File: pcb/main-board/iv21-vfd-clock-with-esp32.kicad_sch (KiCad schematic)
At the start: 24 parts, among them J1 Conn_02x10_Odd_Even, J2 4328, P1 USB_C_Plug_USB2.0, SW1 SW_SPST, SW2 SW_SPST, U1 MAX6921AQI_, U2 MOUDLE-SEEEDUINO-XIAO-ESP32C3, U3 AP3012, U4 S-1167B24

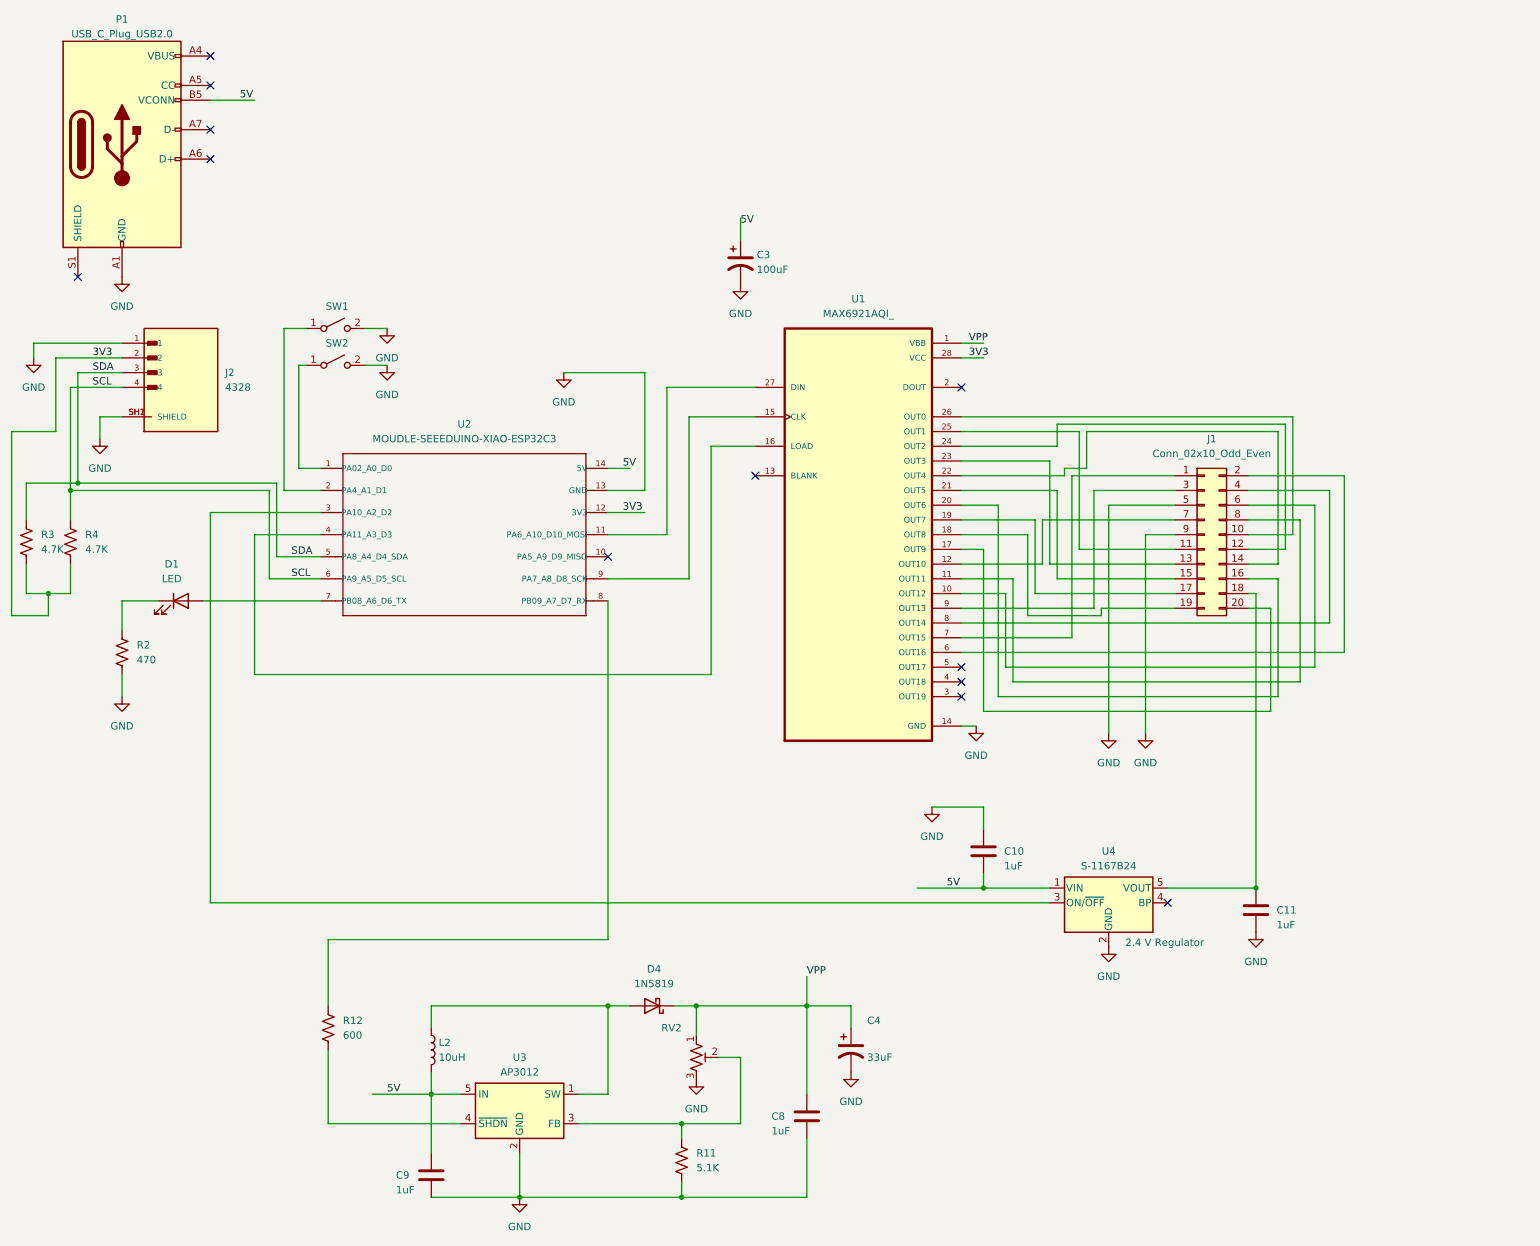
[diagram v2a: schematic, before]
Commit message: Move USB-C port closer to edge of board. Move USB-C port schematic symbol to inside of drawing border.
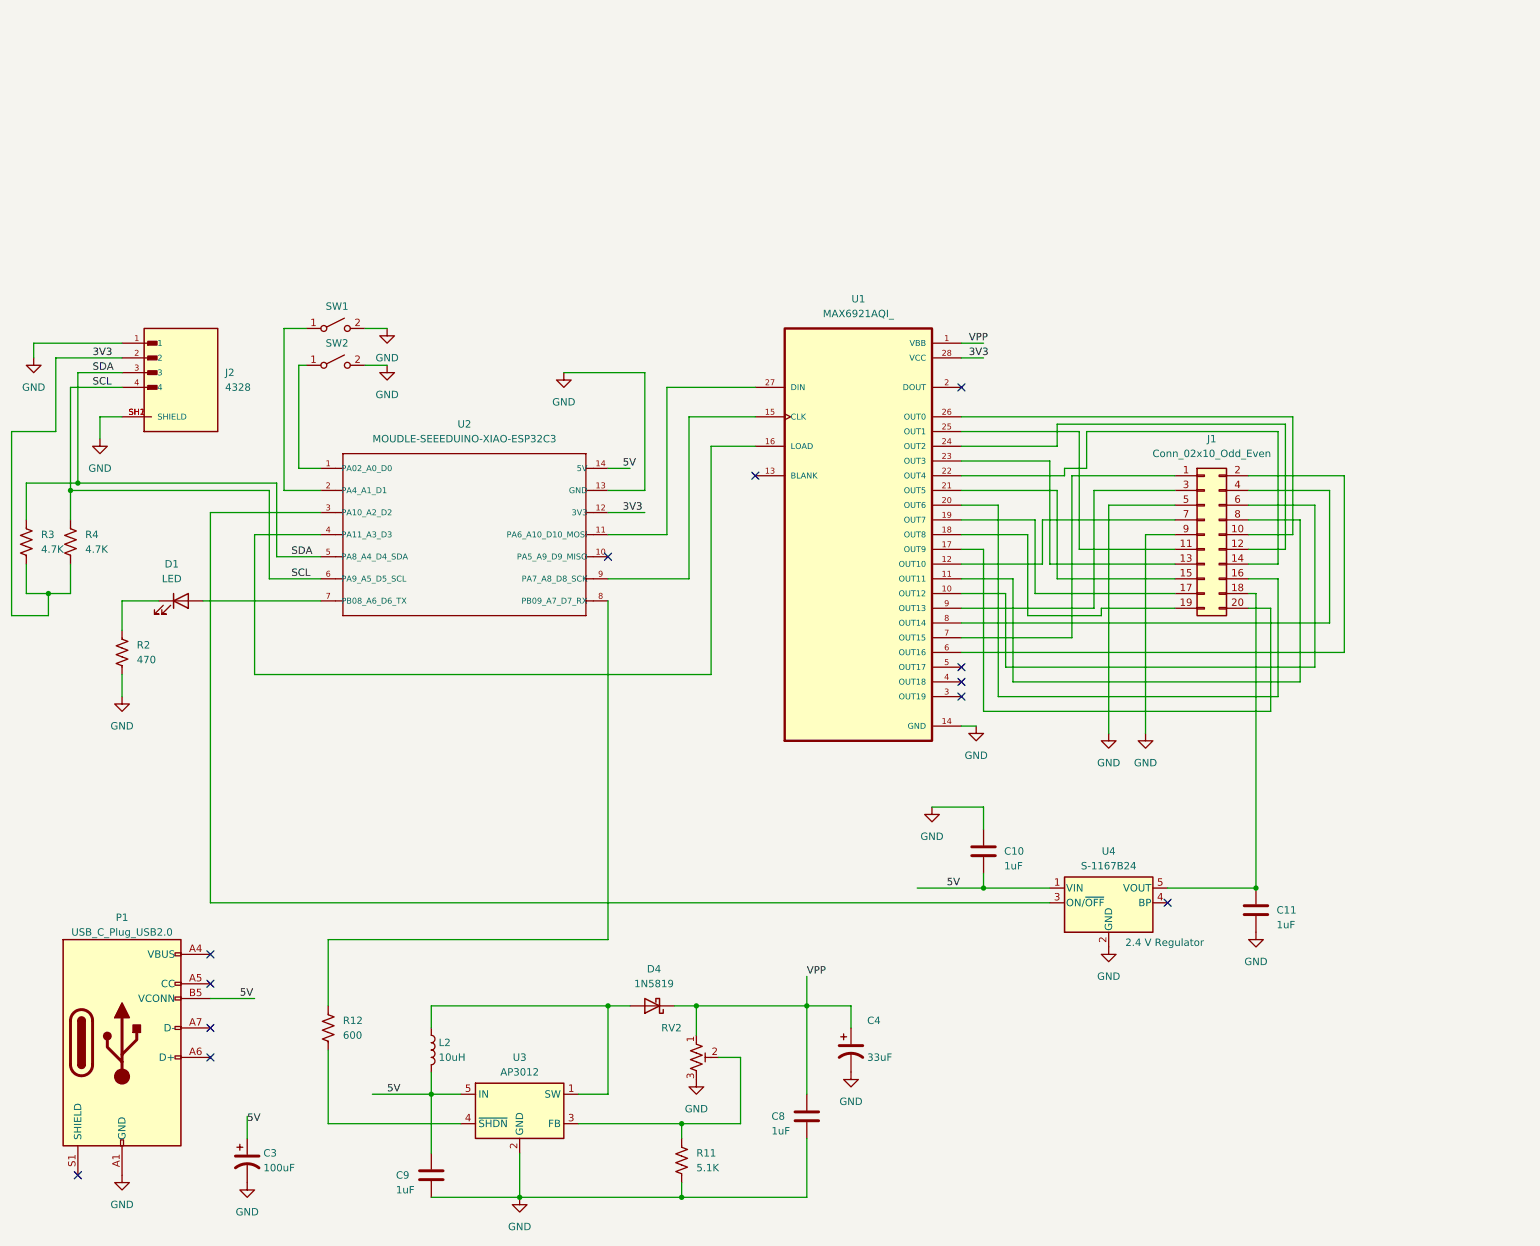
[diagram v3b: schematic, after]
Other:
- moved on the sheet: C3, P1
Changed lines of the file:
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@@
 	)
 	(no_connect
-		(at 48.26 7.62)
+		(at 48.26 162.56)
 	)
 	(no_connect
-		(at 25.4 27.94)
+		(at 25.4 182.88)
 	)
 	(no_connect
@@
 	)
 	(no_connect
-		(at 48.26 2.54)
+		(at 48.26 157.48)
 	)
 	(no_connect
@@
 	)
 	(no_connect
-		(at 48.26 -5.08)
+		(at 48.26 149.86)
 	)
 	(no_connect
-		(at 48.26 -10.16)
+		(at 48.26 144.78)
 	)
 	(no_connect
@@
 	(wire
 		(pts
-			(xy 139.7 17.78) (xy 139.7 21.59)
+			(xy 54.61 172.72) (xy 54.61 176.53)
 		)
 		(stroke
@@
 	(wire
 		(pts
-			(xy 48.26 -2.54) (xy 55.88 -2.54)
+			(xy 48.26 152.4) (xy 55.88 152.4)
 		)
 		(stroke
@@
 	)
 	(label "5V"
-		(at 53.34 -2.54 0)
+		(at 53.34 152.4 0)
 		(effects
 			(font
@@
 	)
 	(label "5V"
-		(at 139.7 19.05 0)
+		(at 54.61 173.99 0)
 		(effects
 			(font
@@
 	(symbol
 		(lib_id "power:GND")
-		(at 33.02 27.94 0)
+		(at 33.02 182.88 0)
 		(unit 1)
 		(exclude_from_sim no)
@@
 		(fields_autoplaced yes)
 		(property "Reference" "#PWR020"
-			(at 33.02 34.29 0)
+			(at 33.02 189.23 0)
 			(effects
 				(font
@@
 		)
 		(property "Value" "GND"
-			(at 33.02 33.02 0)
+			(at 33.02 187.96 0)
 			(effects
 				(font
@@
 		)
 		(property "Footprint" ""
-			(at 33.02 27.94 0)
+			(at 33.02 182.88 0)
 			(effects
 				(font
@@
 		)
 		(property "Datasheet" ""
-			(at 33.02 27.94 0)
+			(at 33.02 182.88 0)
 			(effects
 				(font
@@
 		)
 		(property "Description" "Power symbol creates a global label with name \"GND\" , ground"
-			(at 33.02 27.94 0)
+			(at 33.02 182.88 0)
 			(effects
 				(font
@@
 	(symbol
 		(lib_id "Connector:USB_C_Plug_USB2.0")
-		(at 33.02 5.08 0)
+		(at 33.02 160.02 0)
 		(unit 1)
 		(exclude_from_sim no)
@@
 		(fields_autoplaced yes)
 		(property "Reference" "P1"
-			(at 33.02 -16.51 0)
+			(at 33.02 138.43 0)
 			(effects
 				(font
@@
 		)
 		(property "Value" "USB_C_Plug_USB2.0"
-			(at 33.02 -13.97 0)
+			(at 33.02 140.97 0)
 			(effects
 				(font
@@
 		)
 		(property "Footprint" "Connector_USB:USB_C_Receptacle_GCT_USB4105-xx-A_16P_TopMnt_Horizontal"
-			(at 36.83 5.08 0)
+			(at 36.83 160.02 0)
 			(effects
 				(font
@@
 		)
 		(property "Datasheet" "https://www.usb.org/sites/default/files/documents/usb_type-c.zip"
-			(at 36.83 5.08 0)
+			(at 36.83 160.02 0)
 			(effects
 				(font
@@
 		)
 		(property "Description" "USB 2.0-only Type-C Plug connector"
-			(at 33.02 5.08 0)
+			(at 33.02 160.02 0)
 			(effects
 				(font
@@
 	(symbol
 		(lib_id "Device:C_Polarized_US")
-		(at 139.7 25.4 0)
+		(at 54.61 180.34 0)
 		(unit 1)
 		(exclude_from_sim no)
@@
 		(dnp no)
 		(property "Reference" "C3"
-			(at 142.494 24.13 0)
+			(at 57.404 179.07 0)
 			(effects
 				(font
@@
 		)
 		(property "Value" "100uF"
-			(at 142.494 26.67 0)
+			(at 57.404 181.61 0)
 			(effects
 				(font
@@
 		)
 		(property "Footprint" "Capacitor_SMD:CP_Elec_8x10.5"
-			(at 139.7 25.4 0)
+			(at 54.61 180.34 0)
 			(effects
 				(font
@@
 		)
 		(property "Datasheet" "~"
-			(at 139.7 25.4 0)
+			(at 54.61 180.34 0)
 			(effects
 				(font
@@
 		)
 		(property "Description" "Polarized capacitor, US symbol"
-			(at 139.7 25.4 0)
+			(at 54.61 180.34 0)
 			(effects
 				(font
@@
 	(symbol
 		(lib_id "power:GND")
-		(at 139.7 29.21 0)
+		(at 54.61 184.15 0)
 		(unit 1)
 		(exclude_from_sim no)
@@
 		(fields_autoplaced yes)
 		(property "Reference" "#PWR016"
-			(at 139.7 35.56 0)
+			(at 54.61 190.5 0)
 			(effects
 				(font
@@
 		)
 		(property "Value" "GND"
-			(at 139.7 34.29 0)
+			(at 54.61 189.23 0)
 			(effects
 				(font
@@
 		)
 		(property "Footprint" ""
-			(at 139.7 29.21 0)
+			(at 54.61 184.15 0)
 			(effects
 				(font
@@
 		)
 		(property "Datasheet" ""
-			(at 139.7 29.21 0)
+			(at 54.61 184.15 0)
 			(effects
 				(font
@@
 		)
 		(property "Description" "Power symbol creates a global label with name \"GND\" , ground"
-			(at 139.7 29.21 0)
+			(at 54.61 184.15 0)
 			(effects
 				(font

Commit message: - Add details to electrolytic capacitor components. - No-fill zone for inductor footprint
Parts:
- C3: Product URL (none) -> https://www.mouser.com/ProductDetail/581-AHA0810101M035R; Voltage Rating (none) -> 35V DC
- C4: Product URL (none) -> https://www.mouser.com/ProductDetail/581-AHA0810330M063R; Voltage Rating (none) -> 63V DC
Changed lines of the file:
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@@
 			)
 		)
-		(property "Datasheet" "~"
+		(property "Datasheet" "https://www.mouser.com/datasheet/2/40/kyocera_avx_aha_series-2887216.pdf"
 			(at 54.61 180.34 0)
 			(effects
@@
 		)
 		(property "Description" "Polarized capacitor, US symbol"
+			(at 54.61 180.34 0)
+			(effects
+				(font
+					(size 1.27 1.27)
+				)
+				(hide yes)
+			)
+		)
+		(property "Voltage Rating" "35V DC"
+			(at 54.61 180.34 0)
+			(effects
+				(font
+					(size 1.27 1.27)
+				)
+				(hide yes)
+			)
+		)
+		(property "Product URL" "https://www.mouser.com/ProductDetail/581-AHA0810101M035R"
 			(at 54.61 180.34 0)
 			(effects
@@
 			)
 		)
-		(property "Datasheet" "~"
+		(property "Datasheet" "https://www.mouser.com/datasheet/2/40/kyocera_avx_aha_series-2887216.pdf"
 			(at 158.75 161.29 0)
 			(effects
@@
 			(at 158.75 161.29 0)
 			(effects
+				(font
+					(size 1.27 1.27)
+				)
+				(hide yes)
+			)
+		)
+		(property "Voltage Rating" "63V DC"
+			(at 158.75 161.29 0)
+			(effects
+				(font
+					(size 1.27 1.27)
+				)
+				(hide yes)
+			)
+		)
+		(property "Product URL" "https://www.mouser.com/ProductDetail/581-AHA0810330M063R"
+			(at 158.75 161.29 0)
+			(effects

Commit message: Update some footprints and symbols in schematic.
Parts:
- P1: Product URL (none) -> https://www.mouser.com/ProductDetail/179-UJ20CHGSMT1P16TR
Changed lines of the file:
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@@
 			)
 		)
-		(property "Datasheet" "https://www.usb.org/sites/default/files/documents/usb_type-c.zip"
+		(property "Datasheet" "https://www.mouser.com/datasheet/2/1628/uj20_c_h_g_smt_1_p16_tr-3511223.pdf"
 			(at 36.83 160.02 0)
 			(effects
@@
 		)
 		(property "Description" "USB 2.0-only Type-C Plug connector"
+			(at 33.02 160.02 0)
+			(effects
+				(font
+					(size 1.27 1.27)
+				)
+				(hide yes)
+			)
+		)
+		(property "Product URL" "https://www.mouser.com/ProductDetail/179-UJ20CHGSMT1P16TR"
 			(at 33.02 160.02 0)
 			(effects
@@
 		(dnp no)
 		(property "Reference" "RV2"
-			(at 129.54 157.4799 0)
+			(at 129.032 161.29 0)
 			(effects
 				(font
@@
 		)
 		(property "Value" "100K"
-			(at 149.606 170.18 0)
+			(at 129.54 163.5761 0)
 			(effects
 				(font
@@
 				)
 				(justify right)
-				(hide yes)
-			)
-		)
+			)
+		)

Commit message: ...
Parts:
- L2: footprint Inductor_THT:L_Radial_D12.0mm_P5.00mm_Fastron_11P -> Inductor_THT:L_Radial_D7.5mm_P3.50mm_Fastron_07P
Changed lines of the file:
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@@
 			)
 		)
-		(property "Footprint" "Inductor_THT:L_Radial_D12.0mm_P5.00mm_Fastron_11P"
+		(property "Footprint" "Inductor_THT:L_Radial_D7.5mm_P3.50mm_Fastron_07P"
 			(at 86.36 161.29 0)
 			(effects

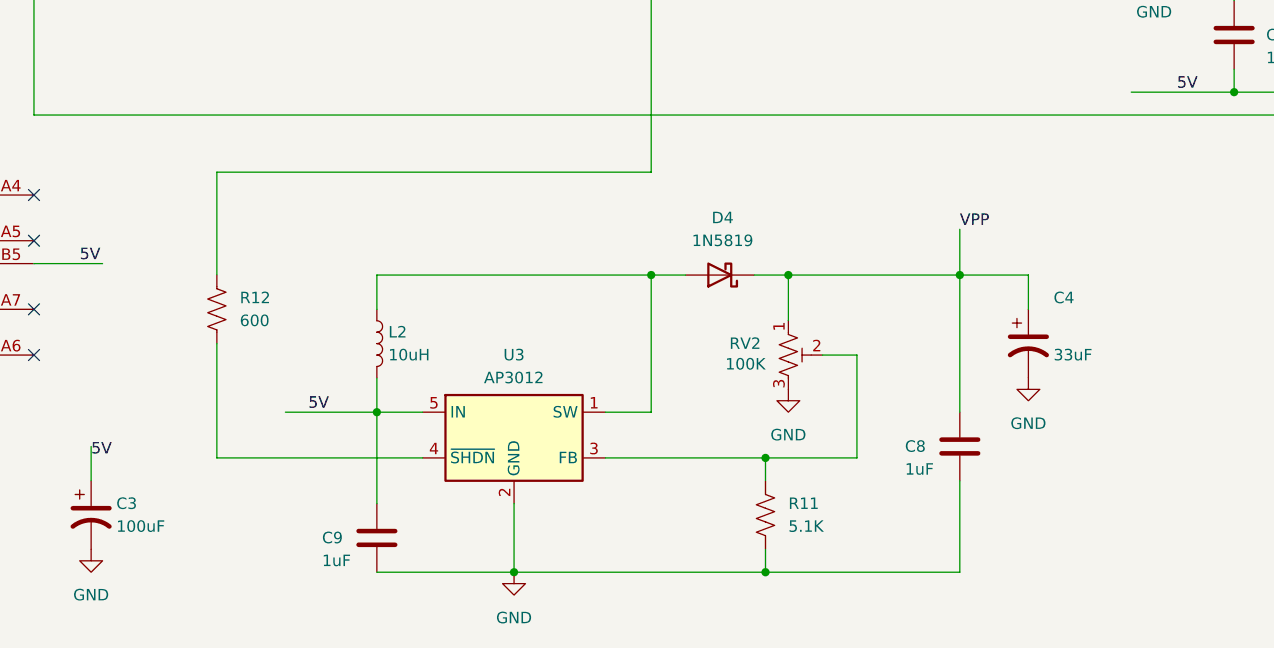
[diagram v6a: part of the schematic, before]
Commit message: Some components PCB rearanging.
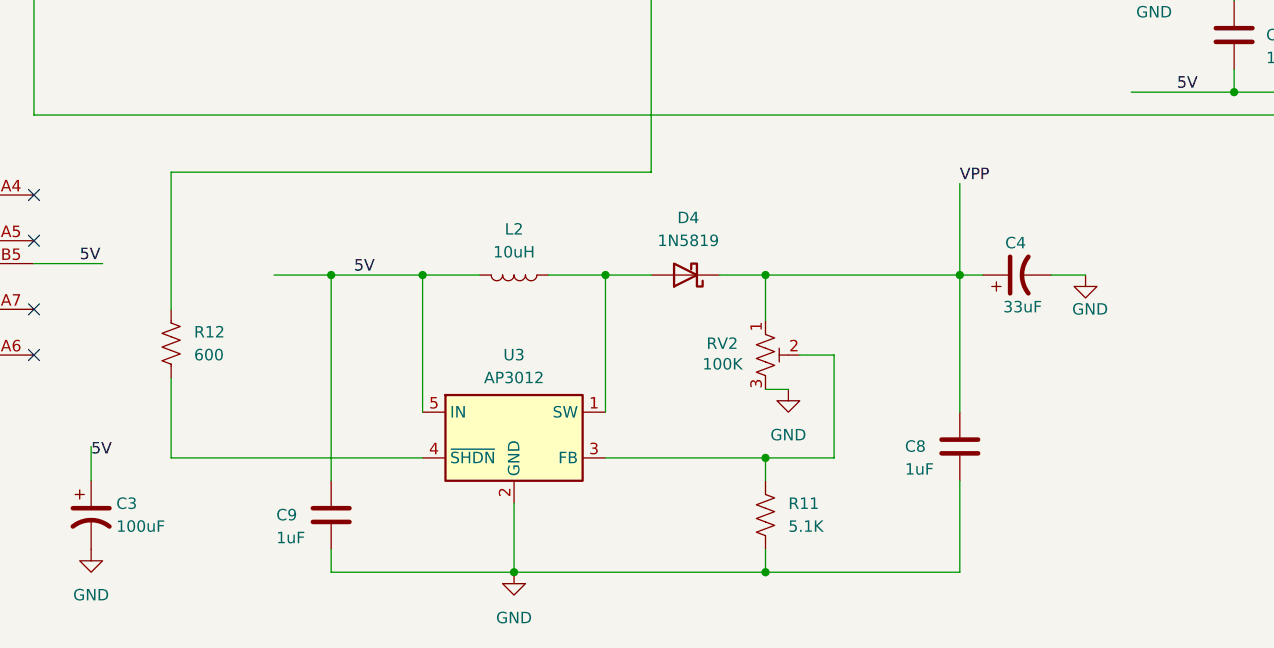
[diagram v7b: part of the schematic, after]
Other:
- moved on the sheet: C4, C9, D4, L2, R12, RV2
